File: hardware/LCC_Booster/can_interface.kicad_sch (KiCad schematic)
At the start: 3 parts, among them U42 MCP2515-xSO, U43 MCP2562-E-SN, Y1 16.0 MHz, 22pF

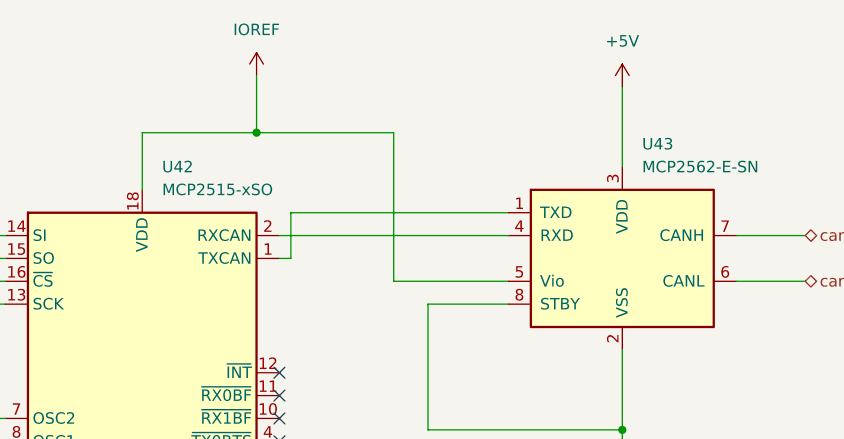
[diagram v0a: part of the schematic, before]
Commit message: Switch to single Arduino per board
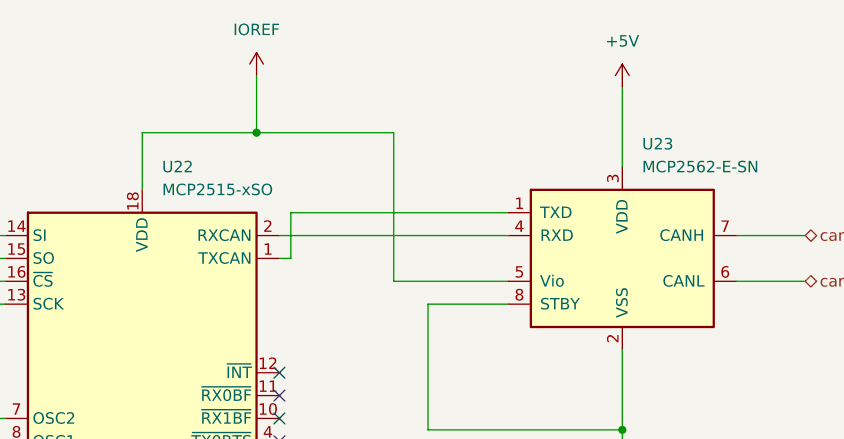
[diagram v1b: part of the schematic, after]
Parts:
- renumbered U42 to U22, U43 to U23
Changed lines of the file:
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@@
 		(dnp no)
 		(fields_autoplaced yes)
-		(property "Reference" "#PWR089"
+		(property "Reference" "#PWR052"
 			(at 186.69 138.43 0)
 			(effects
@@
 		)
 		(instances
-			(project "Arduino_Nano_LCC_Boosters"
-				(path "/fe98a12a-bd47-40d6-885d-b688d74230c5/cd83ab7d-0ee3-4612-a533-ef6c7ffe8ed9"
-					(reference "#PWR089")
-					(unit 1)
-				)
-				(path "/fe98a12a-bd47-40d6-885d-b688d74230c5/577d4ac4-b29d-4707-bc46-b8b7b8fe12a7"
-					(reference "#PWR092")
+			(project "LCC_Booster"
+				(path "/e8524381-bb01-4107-93ec-8133e878a3da/b324a729-c370-420a-b992-28ea70226130"
+					(reference "#PWR052")
 					(unit 1)
 				)
@@
 		)
 		(instances
-			(project "Arduino_Nano_LCC_Boosters"
-				(path "/fe98a12a-bd47-40d6-885d-b688d74230c5/cd83ab7d-0ee3-4612-a533-ef6c7ffe8ed9"
+			(project "LCC_Booster"
+				(path "/e8524381-bb01-4107-93ec-8133e878a3da/b324a729-c370-420a-b992-28ea70226130"
 					(reference "Y1")
-					(unit 1)
-				)
-				(path "/fe98a12a-bd47-40d6-885d-b688d74230c5/577d4ac4-b29d-4707-bc46-b8b7b8fe12a7"
-					(reference "Y2")
 					(unit 1)
 				)
@@
 		(dnp no)
 		(fields_autoplaced yes)
-		(property "Reference" "#PWR087"
+		(property "Reference" "#PWR050"
 			(at 146.05 63.5 0)
 			(effects
@@
 		)
 		(instances
-			(project "Arduino_Nano_LCC_Boosters"
-				(path "/fe98a12a-bd47-40d6-885d-b688d74230c5/cd83ab7d-0ee3-4612-a533-ef6c7ffe8ed9"
-					(reference "#PWR087")
-					(unit 1)
-				)
-				(path "/fe98a12a-bd47-40d6-885d-b688d74230c5/577d4ac4-b29d-4707-bc46-b8b7b8fe12a7"
-					(reference "#PWR090")
+			(project "LCC_Booster"
+				(path "/e8524381-bb01-4107-93ec-8133e878a3da/b324a729-c370-420a-b992-28ea70226130"
+					(reference "#PWR050")
 					(unit 1)
 				)
@@
 		(dnp no)
 		(fields_autoplaced yes)
-		(property "Reference" "U42"
+		(property "Reference" "U22"
 			(at 135.5441 69.85 0)
 			(effects
@@
 		)
 		(instances
-			(project "Arduino_Nano_LCC_Boosters"
-				(path "/fe98a12a-bd47-40d6-885d-b688d74230c5/cd83ab7d-0ee3-4612-a533-ef6c7ffe8ed9"
-					(reference "U42")
-					(unit 1)
-				)
-				(path "/fe98a12a-bd47-40d6-885d-b688d74230c5/577d4ac4-b29d-4707-bc46-b8b7b8fe12a7"
-					(reference "U44")
+			(project "LCC_Booster"
+				(path "/e8524381-bb01-4107-93ec-8133e878a3da/b324a729-c370-420a-b992-28ea70226130"
+					(reference "U22")
 					(unit 1)
 				)
@@
 		(dnp no)
 		(fields_autoplaced yes)
-		(property "Reference" "U43"
+		(property "Reference" "U23"
 			(at 188.8841 67.31 0)
 			(effects
@@
 		)
 		(instances
-			(project "Arduino_Nano_LCC_Boosters"
-				(path "/fe98a12a-bd47-40d6-885d-b688d74230c5/cd83ab7d-0ee3-4612-a533-ef6c7ffe8ed9"
-					(reference "U43")
-					(unit 1)
-				)
-				(path "/fe98a12a-bd47-40d6-885d-b688d74230c5/577d4ac4-b29d-4707-bc46-b8b7b8fe12a7"
-					(reference "U45")
+			(project "LCC_Booster"
+				(path "/e8524381-bb01-4107-93ec-8133e878a3da/b324a729-c370-420a-b992-28ea70226130"
+					(reference "U23")
 					(unit 1)
 				)
@@
 		(dnp no)
 		(fields_autoplaced yes)
-		(property "Reference" "#PWR088"
+		(property "Reference" "#PWR051"
 			(at 186.69 64.77 0)
 			(effects
@@
 		)
 		(instances
-			(project "Arduino_Nano_LCC_Boosters"
-				(path "/fe98a12a-bd47-40d6-885d-b688d74230c5/cd83ab7d-0ee3-4612-a533-ef6c7ffe8ed9"
-					(reference "#PWR088")
-					(unit 1)
-				)
-				(path "/fe98a12a-bd47-40d6-885d-b688d74230c5/577d4ac4-b29d-4707-bc46-b8b7b8fe12a7"
-					(reference "#PWR091")
-					(unit 1)
-				)
+			(project "LCC_Booster"
+				(path "/e8524381-bb01-4107-93ec-8133e878a3da/b324a729-c370-420a-b992-28ea70226130"
+					(reference "#PWR051")
+					(unit 1)
+				)

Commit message: LCC Command Station Shield
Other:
- company: (none) -> TMRC
- title: (none) -> Arduino Nano LCC Booster
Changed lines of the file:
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@@
 	(generator_version "8.0")
 	(paper "A4")
+	(title_block
+		(title "Arduino Nano LCC Booster")
+		(date "2024-04-28")
+		(rev "1.0")
+		(company "TMRC")
+		(comment 1 "Noah Paladino")
+	)
 	(junction
 		(at 146.05 66.04)

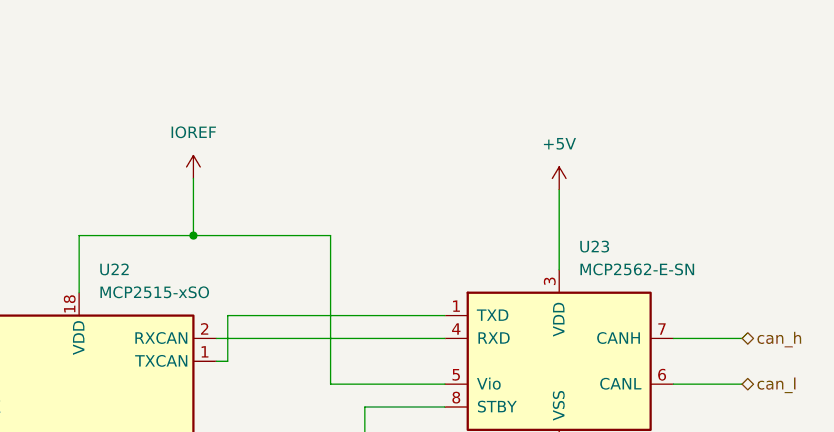
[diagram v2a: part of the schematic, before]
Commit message: Regenerate LCC Booster Gerbers with More Power Filtering
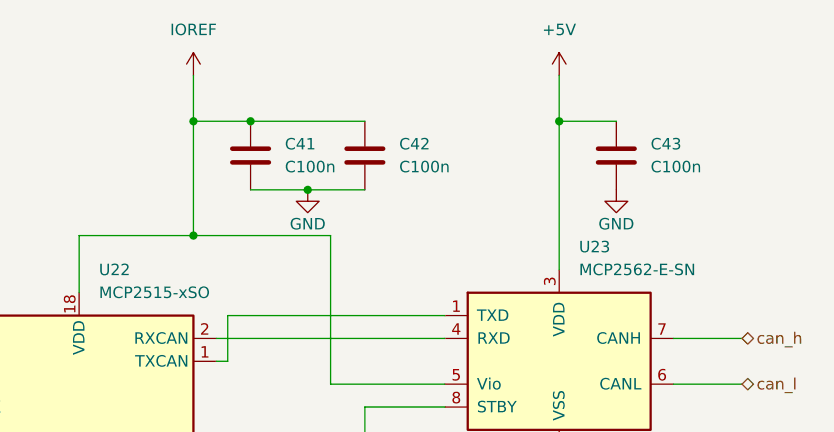
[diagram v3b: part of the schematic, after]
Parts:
- added C41, C42, C43: C100n, Capacitor_SMD:C_0402_1005Metric_Pad0.74x0.62mm_HandSolder, symbol Device:C
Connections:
- net +5V: now also C43.1
- net GND: now also C41.2, C42.2, C43.2
- net IOREF: now also C41.1, C42.1

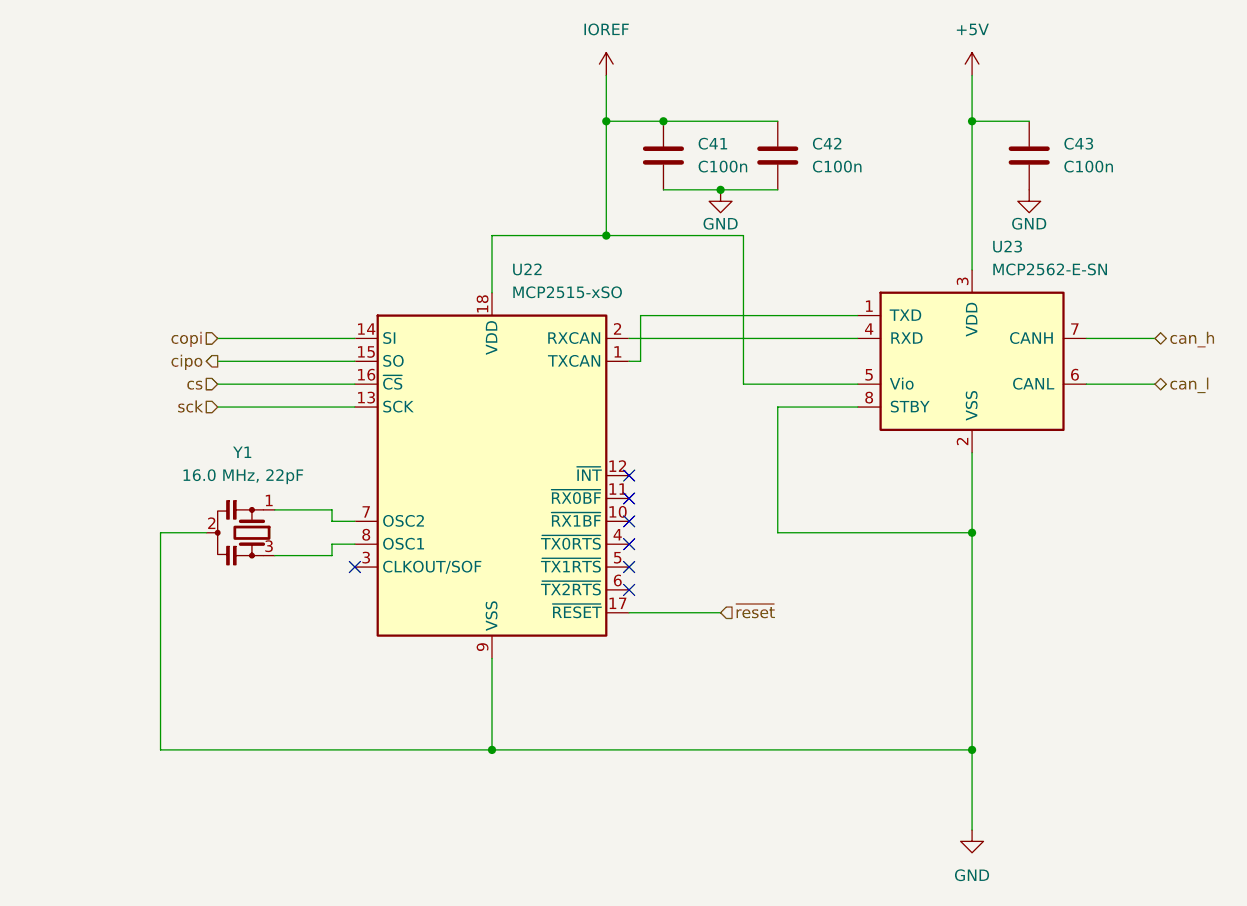
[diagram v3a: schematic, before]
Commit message: Start to work on code structure and added MCP2515 interrupt
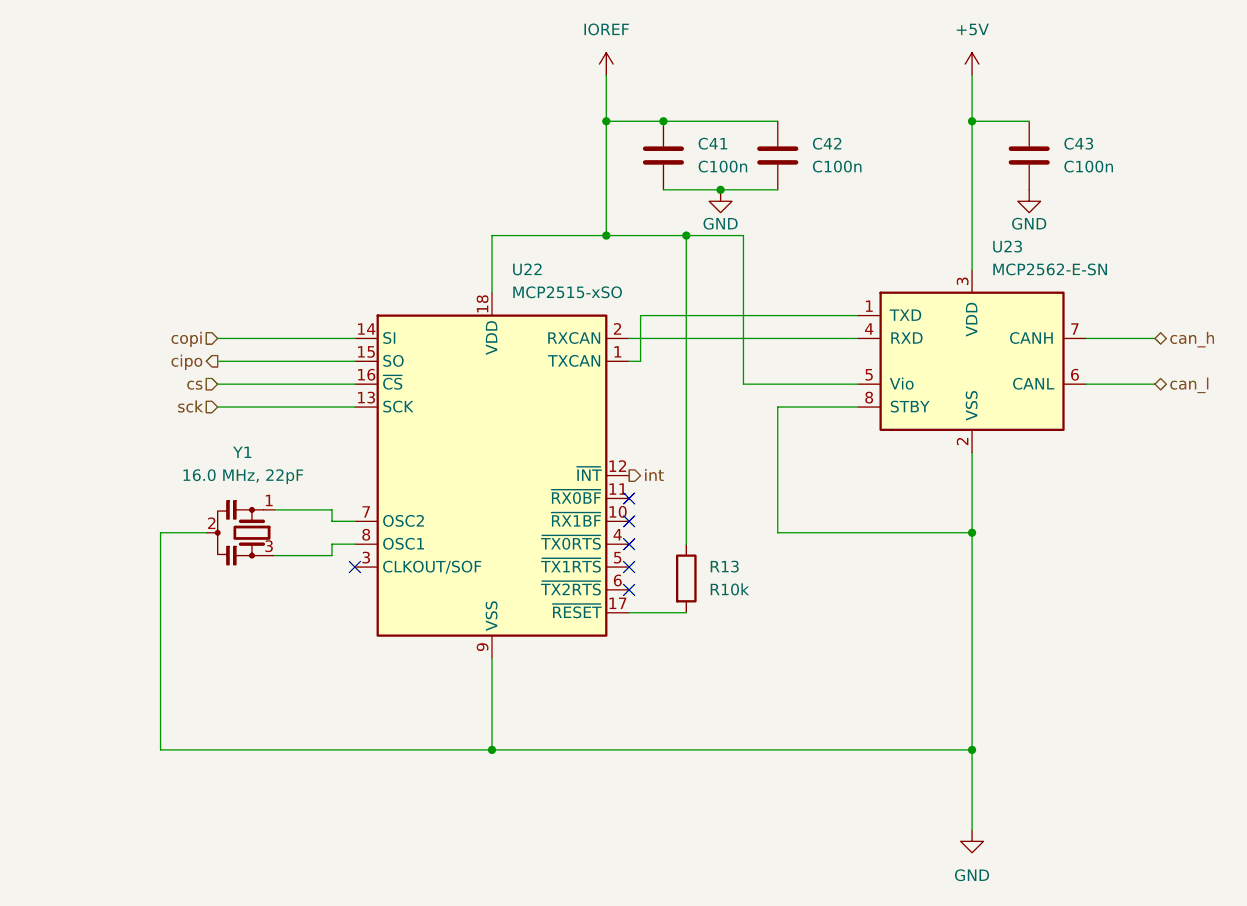
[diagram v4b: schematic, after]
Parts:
- added R13: R10k, Resistor_SMD:R_01005_0402Metric_Pad0.57x0.30mm_HandSolder, symbol Device:R
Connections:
- net IOREF: now also R13.1
- net int: now reaches U22.12 (~{INT})
- net ~{reset}: no longer names the net of U22.17 (~{RESET})
- net ~{reset}: now also R13.2
- no-connect marks 7 -> 6
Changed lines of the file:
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@@
+	)
+	(junction
+		(at 154.94 66.04)
+		(diameter 0)
+		(color 0 0 0 0)
 	)
 	(junction
@@
 	)
 	(no_connect
-		(at 148.59 92.71)
-	)
-	(no_connect
 		(at 148.59 95.25)
 	)
@@
 	(wire
 		(pts
+			(xy 154.94 66.04) (xy 161.29 66.04)
+		)
+		(stroke
+			(width 0)
+			(type default)
+		)
+	)
+	(wire
+		(pts
 			(xy 186.69 53.34) (xy 193.04 53.34)
 		)
@@
 	(wire
 		(pts
-			(xy 158.75 107.95) (xy 148.59 107.95)
+			(xy 148.59 107.95) (xy 154.94 107.95)
 		)
 		(stroke
@@
 	(wire
 		(pts
+			(xy 154.94 66.04) (xy 154.94 100.33)
+		)
+		(stroke
+			(width 0)
+			(type default)
+		)
+	)
+	(wire
+		(pts
 			(xy 186.69 99.06) (xy 165.1 99.06)
 		)
@@
 	(wire
 		(pts
-			(xy 146.05 66.04) (xy 161.29 66.04)
+			(xy 146.05 66.04) (xy 154.94 66.04)
 		)
 		(stroke
@@
 		)
 	)
-	(hierarchical_label "~{reset}"
-		(shape input)
-		(at 158.75 107.95 0)
-		(fields_autoplaced yes)
-		(effects
-			(font
-				(size 1.27 1.27)
-			)
-			(justify left)
-		)
-	)
 	(hierarchical_label "copi"
 		(shape input)
@@
 		)
 	)
+	(hierarchical_label "int"
+		(shape output)
+		(at 148.59 92.71 0)
+		(fields_autoplaced yes)
+		(effects
+			(font
+				(size 1.27 1.27)
+			)
+			(justify left)
+		)
+	)
+	(symbol
+		(lib_id "Device:R")
+		(at 154.94 104.14 0)
+		(unit 1)
+		(exclude_from_sim no)
+		(in_bom yes)
+		(on_board yes)
+		(dnp no)
+		(fields_autoplaced yes)
+		(property "Reference" "R13"
+			(at 157.48 102.8699 0)
+			(effects
+				(font
+					(size 1.27 1.27)
+				)
+				(justify left)
+			)
+		)
+		(property "Value" "R10k"
+			(at 157.48 105.4099 0)
+			(effects
+				(font
+					(size 1.27 1.27)
+				)
+				(justify left)
+			)
+		)
+		(property "Footprint" "Resistor_SMD:R_01005_0402Metric_Pad0.57x0.30mm_HandSolder"
+			(at 153.162 104.14 90)
+			(effects
+				(font
+					(size 1.27 1.27)
+				)
+				(hide yes)
+			)
+		)
+		(property "Datasheet" "~"
+			(at 154.94 104.14 0)
+			(effects
+				(font
+					(size 1.27 1.27)
+				)
+				(hide yes)
+			)
+		)
+		(property "Description" "Resistor"
+			(at 154.94 104.14 0)
+			(effects
+				(font
+					(size 1.27 1.27)
+				)
+				(hide yes)
+			)
+		)
+		(pin "1"
+		)
+		(pin "2"
+		)
+		(instances
+			(project "LCC_Booster"
+				(path "/e8524381-bb01-4107-93ec-8133e878a3da/b324a729-c370-420a-b992-28ea70226130"
+					(reference "R13")
+					(unit 1)
+				)
+			)
+		)
+	)

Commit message: Better Solder Jumpers, Better Pizza
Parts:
- removed R13: R10k, Resistor_SMD:R_01005_0402Metric_Pad0.57x0.30mm_HandSolder, symbol Device:R
- removed U22: MCP2515-xSO, Package_SO:SOIC-18W_7.5x11.6mm_P1.27mm, symbol Interface_CAN_LIN:MCP2515-xSO
- removed Y1: 16.0 MHz, 22pF, Crystal:Crystal_HC49-U-3Pin_Vertical, symbol Device:Resonator_Small
- added C44, C45: C22p, Capacitor_SMD:C_0402_1005Metric_Pad0.74x0.62mm_HandSolder, symbol Device:C
- added JP3, JP4: SolderJumper_3_Bridged12, Jumper:SolderJumper-3_P1.3mm_Bridged12_RoundedPad1.0x1.5mm_NumberLabels, symbol Jumper:SolderJumper_3_Bridged12
- added U22: MCP2518FD-xQBB, Package_SO:SOIC-14_3.9x8.7mm_P1.27mm, symbol Interface_CAN_LIN:MCP2518FD-xQBB
- added Y1: ECS-400-20-46X, ECS_400_20_46X:XTAL_ECS-400-20-46X, symbol ECS-400-20-46X:ECS-400-20-46X
- C41: now not fitted
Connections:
- net GND: now also C44.1, C45.1, U22.15 (VSS), U22.7 (VSS)
- net IOREF: now also U22.14 (VDD)
- net cipo: now also U22.12 (SDO)
- net copi: now also U22.11 (SDI)
- net sck: now also U22.10 (SCK)
- net at U23.1 (TXD): now also JP4.3 (B), U22.1 (TXCAN)
- net at U23.4 (RXD): now also JP3.3 (B), U22.2 (RXCAN)
- new net: C44.2, U22.5 (OSC2), Y1.2
- new net: JP4.1 (A), U22.4 (~{INT})
- new net: JP3.1 (A), U22.13 (~{CS})
- new net: C45.2, U22.6 (OSC1), Y1.1
- new net cs_canrx: JP3.2 (C)
- new net int_cantx: JP4.2 (C)
- no-connect marks 6 -> 3

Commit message: Update to hardware v2 and cleanup
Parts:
- renumbered C44 to C29, C45 to C30, C41 to C31, C42 to C32, C43 to C33, JP3 to JP8, JP4 to JP9, U22 to U11, U23 to U12
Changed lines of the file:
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@@
 	(title_block
 		(title "Arduino Nano LCC Booster")
-		(date "2024-04-28")
-		(rev "1.0")
+		(date "2024-05-14")
+		(rev "2")
 		(company "TMRC")
 		(comment 1 "Noah Paladino")
@@
 		(on_board yes)
 		(dnp yes)
-		(property "Reference" "C44"
+		(property "Reference" "C29"
 			(at 105.41 94.742 90)
 			(effects
@@
 			(project "LCC_Booster"
 				(path "/e8524381-bb01-4107-93ec-8133e878a3da/b324a729-c370-420a-b992-28ea70226130"
-					(reference "C44")
+					(reference "C29")
 					(unit 1)
 				)
@@
 		(dnp no)
 		(fields_autoplaced yes)
-		(property "Reference" "#PWR053"
+		(property "Reference" "#PWR052"
 			(at 186.69 138.43 0)
 			(effects
@@
 			(project "LCC_Booster"
 				(path "/e8524381-bb01-4107-93ec-8133e878a3da/b324a729-c370-420a-b992-28ea70226130"
-					(reference "#PWR053")
+					(reference "#PWR052")
 					(unit 1)
 				)
@@
 		(on_board yes)
 		(dnp no)
-		(property "Reference" "JP4"
+		(property "Reference" "JP9"
 			(at 152.4 86.3601 0)
 			(effects
@@
 			(project "LCC_Booster"
 				(path "/e8524381-bb01-4107-93ec-8133e878a3da/b324a729-c370-420a-b992-28ea70226130"
-					(reference "JP4")
+					(reference "JP9")
 					(unit 1)
 				)
@@
 		(on_board yes)
 		(dnp no)
-		(property "Reference" "#PWR054"
+		(property "Reference" "#PWR053"
 			(at 193.04 67.31 0)
 			(effects
@@
 			(project "LCC_Booster"
 				(path "/e8524381-bb01-4107-93ec-8133e878a3da/b324a729-c370-420a-b992-28ea70226130"
-					(reference "#PWR054")
+					(reference "#PWR053")
 					(unit 1)
 				)
@@
 		(on_board yes)
 		(dnp no)
-		(property "Reference" "JP3"
+		(property "Reference" "JP8"
 			(at 106.68 69.8501 0)
 			(effects
@@
 			(project "LCC_Booster"
 				(path "/e8524381-bb01-4107-93ec-8133e878a3da/b324a729-c370-420a-b992-28ea70226130"
-					(reference "JP3")
+					(reference "JP8")
 					(unit 1)
 				)
@@
 		(dnp no)
 		(fields_autoplaced yes)
-		(property "Reference" "#PWR050"
+		(property "Reference" "#PWR049"
 			(at 146.05 52.07 0)
 			(effects
@@
 			(project "LCC_Booster"
 				(path "/e8524381-bb01-4107-93ec-8133e878a3da/b324a729-c370-420a-b992-28ea70226130"
-					(reference "#PWR050")
+					(reference "#PWR049")
 					(unit 1)
 				)
@@
 		(dnp yes)
 		(fields_autoplaced yes)
-		(property "Reference" "U22"
+		(property "Reference" "U11"
 			(at 135.5441 69.85 0)
 			(effects
@@
 			(project "LCC_Booster"
 				(path "/e8524381-bb01-4107-93ec-8133e878a3da/b324a729-c370-420a-b992-28ea70226130"
-					(reference "U22")
+					(reference "U11")
 					(unit 1)
 				)
@@
 		(dnp no)
 		(fields_autoplaced yes)
-		(property "Reference" "U23"
+		(property "Reference" "U12"
 			(at 188.8841 67.31 0)
 			(effects
@@
 			(project "LCC_Booster"
 				(path "/e8524381-bb01-4107-93ec-8133e878a3da/b324a729-c370-420a-b992-28ea70226130"
-					(reference "U23")
+					(reference "U12")
 					(unit 1)
 				)
@@
 		(on_board yes)
 		(dnp no)
-		(property "Reference" "#PWR051"
+		(property "Reference" "#PWR050"
 			(at 158.75 67.31 0)
 			(effects
@@
 			(project "LCC_Booster"
 				(path "/e8524381-bb01-4107-93ec-8133e878a3da/b324a729-c370-420a-b992-28ea70226130"
-					(reference "#PWR051")
+					(reference "#PWR050")
 					(unit 1)
 				)
@@
 		(dnp yes)
 		(fields_autoplaced yes)
-		(property "Reference" "C41"
+		(property "Reference" "C31"
 			(at 156.21 55.8799 0)
 			(effects
@@
 			(project "LCC_Booster"
 				(path "/e8524381-bb01-4107-93ec-8133e878a3da/b324a729-c370-420a-b992-28ea70226130"
-					(reference "C41")
+					(reference "C31")
 					(unit 1)
 				)
@@
 		(dnp no)
 		(fields_autoplaced yes)
-		(property "Reference" "#PWR052"
+		(property "Reference" "#PWR051"
 			(at 186.69 52.07 0)
 			(effects
@@
 			(project "LCC_Booster"
 				(path "/e8524381-bb01-4107-93ec-8133e878a3da/b324a729-c370-420a-b992-28ea70226130"
-					(reference "#PWR052")
+					(reference "#PWR051")
 					(unit 1)
 				)
@@
 		(on_board yes)
 		(dnp yes)
-		(property "Reference" "C45"
+		(property "Reference" "C30"
 			(at 105.41 104.902 90)
 			(effects
@@
 			(project "LCC_Booster"
 				(path "/e8524381-bb01-4107-93ec-8133e878a3da/b324a729-c370-420a-b992-28ea70226130"
-					(reference "C45")
+					(reference "C30")
 					(unit 1)
 				)
@@
 		(dnp no)
 		(fields_autoplaced yes)
-		(property "Reference" "C43"
+		(property "Reference" "C33"
 			(at 196.85 55.8799 0)
 			(effects
@@
 			(project "LCC_Booster"
 				(path "/e8524381-bb01-4107-93ec-8133e878a3da/b324a729-c370-420a-b992-28ea70226130"
-					(reference "C43")
+					(reference "C33")
 					(unit 1)
 				)
@@
 		(dnp no)
 		(fields_autoplaced yes)
-		(property "Reference" "C42"
+		(property "Reference" "C32"
 			(at 168.91 55.8799 0)
 			(effects
@@
 			(project "LCC_Booster"
 				(path "/e8524381-bb01-4107-93ec-8133e878a3da/b324a729-c370-420a-b992-28ea70226130"
-					(reference "C42")
+					(reference "C32")
 					(unit 1)
 				)
